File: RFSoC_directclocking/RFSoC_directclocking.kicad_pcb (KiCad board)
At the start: 2 copper layers, 57.2 x 38.1 mm, 16 parts, among them U1 TCM2-33WX+, U2 TCM2-33WX+

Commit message: added kicad symbol+footprint
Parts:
- removed R1, R2: 50, Resistor_SMD:R_0402_1005Metric
- removed R3: 100, Resistor_SMD:R_0402_1005Metric
- added U3: EP2RCW+, Mouser:QFN50P500X500X100-33N-D, F.Cu at (94.0, 78.7)
- renumbered clk-in to J1, clkb- to J2, clkb+ to J3, clka- to J4, clka+ to J5
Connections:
- U1 pad 6: Net-(R2-Pad2) -> Net-(U1-Pad6)
- U2 pad 6: Net-(R2-Pad2) -> Net-(U2-Pad6)
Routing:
- net Net-(R2-Pad2): track 10.7 -> 0.00 mm
- net Net-(C1-Pad2): track 18.2 -> 15.8 mm

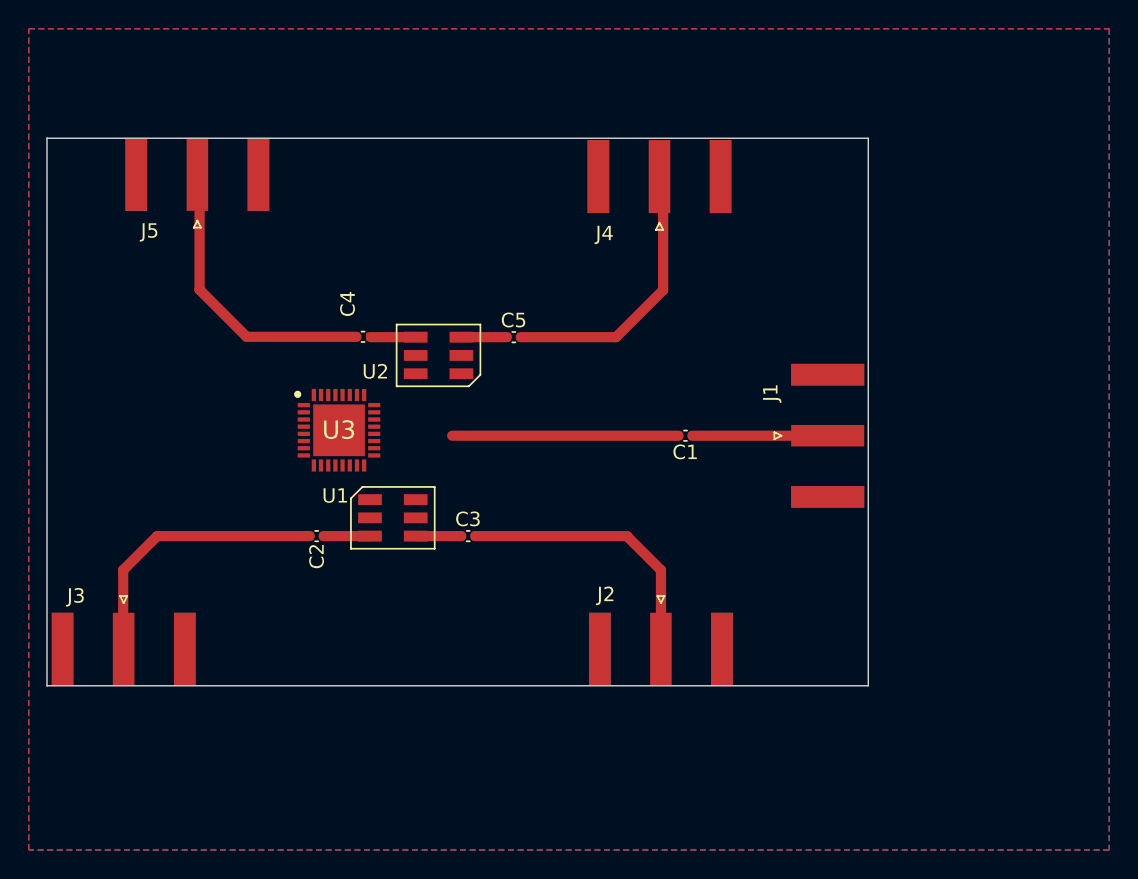
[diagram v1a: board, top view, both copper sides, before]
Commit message: improvements
Made improvement to kicad symbol and replaced footprint for baluns. They
were incorrectly orientated with regards to pin numbering
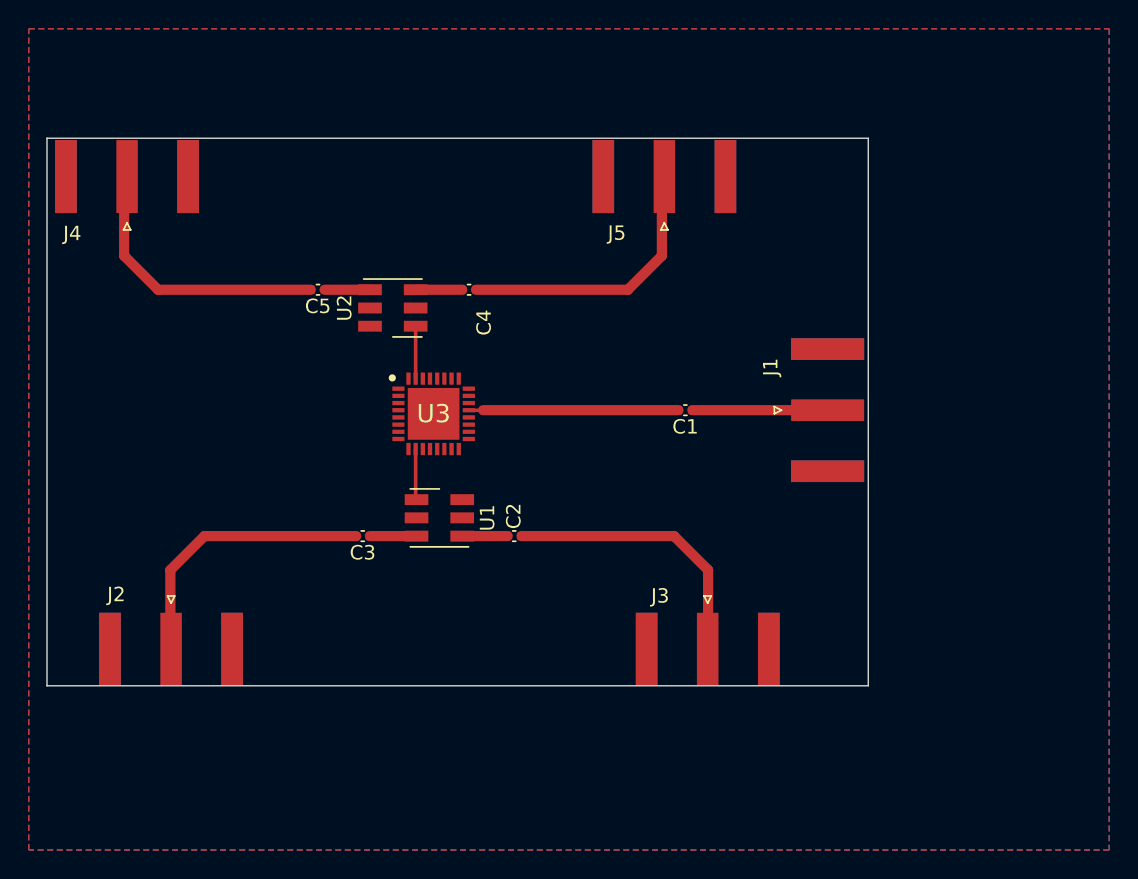
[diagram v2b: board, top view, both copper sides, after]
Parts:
- U1, U2: value TCM2-33WX+ -> Mini-Circuits_DB1627; footprint RF_Mini-Circuits:TCM2-33WX+ -> RF_Mini-Circuits:Mini-Circuits_DB1627
- moved J3 40.6 mm to (119.6, 94.0)
- moved J4 37.0 mm to (79.2, 61.1)
- moved J2 34.1 mm to (82.3, 94.0)
- moved J5 32.5 mm to (116.6, 61.1)
- moved C5 14.0 mm to (92.5, 69.0), turned to 180 degrees
- moved C2 13.7 mm to (106.2, 86.1), turned to 0 degrees
- moved C4 8.07 mm to (103.0, 69.0), turned to 0 degrees
- moved C3 7.34 mm to (95.6, 86.1), turned to 180 degrees
- moved U3 6.68 mm to (100.6, 77.6)
- moved U2 4.58 mm to (97.7, 70.2)
- moved U1 3.24 mm to (101.0, 84.8)
- moved C1 1.78 mm to (118.1, 77.3)
- moved J1 1.78 mm to (128.0, 77.3)
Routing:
- net Net-(U2-Pad6): track 0.00 -> 3.65 mm
- net Net-(U1-Pad6): track 0.00 -> 3.55 mm
- net Net-(C1-Pad2): track 15.8 -> 14.4 mm
- net Net-(C5-Pad2): track 18.9 -> 19.5 mm
- net Net-(C4-Pad2): track 18.9 -> 19.4 mm

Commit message: moved forkem and labeled ports
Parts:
- moved G*** 46.6 mm to (84.9, 77.8)
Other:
- board text added: "CLK_IN"
- board text added: "OUT_N"
- board text added: "OUT_P"
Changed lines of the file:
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@@
   )
   (footprint "LOGO" (layer "B.Cu")
-    (at 131.445 78.74 180)
+    (at 84.8868 77.8002 180)
     (attr board_only exclude_from_pos_files exclude_from_bom)
     (fp_text reference "G***" (at 0.508 3.556) (layer "Dwgs.User")
@@
   (gr_line (start 130.81 96.52) (end 73.66 96.52) (layer "Edge.Cuts") (width 0.1))
   (gr_line (start 73.66 96.52) (end 73.66 58.42) (layer "Edge.Cuts") (width 0.1))
-  (gr_text "fork'em" (at 133.35 78.867 90) (layer "B.SilkS")
+  (gr_text "fork'em" (at 84.7344 81.3562) (layer "B.SilkS")
     (effects (font (size 0.762 0.889) (thickness 0.15)) (justify mirror))
   )
+  (gr_text "OUT_N" (at 86.36 61.1124 90) (layer "F.SilkS")
+    (effects (font (size 1 1) (thickness 0.15)))
+  )
+  (gr_text "OUT_P" (at 109.7788 61.2902 90) (layer "F.SilkS")
+    (effects (font (size 1 1) (thickness 0.15)))
+  )
+  (gr_text "OUT_N" (at 112.9792 93.6752 90) (layer "F.SilkS")
+    (effects (font (size 1 1) (thickness 0.15)))
+  )
+  (gr_text "OUT_P" (at 89.0016 93.7514 90) (layer "F.SilkS")
+    (effects (font (size 1 1) (thickness 0.15)))
+  )
+  (gr_text "CLK_IN" (at 127.6604 71.1454) (layer "F.SilkS")
+    (effects (font (size 1 1) (thickness 0.15)))
+  )
   (segment (start 105.72 86.106) (end 102.494 86.106) (width 0.7112) (layer "F.Cu") (net 1))
